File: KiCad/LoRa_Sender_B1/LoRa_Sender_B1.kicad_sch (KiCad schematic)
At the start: 5 parts, among them J1 Screw_Terminal_01x14, U1 RFM95W-868S2, U2 BME680

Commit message: Start design into KiCAD2
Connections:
- net GND: now also U2.1 (GND), U2.7 (GND)
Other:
- moved on the sheet: R1
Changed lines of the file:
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@@
 (kicad_sch (version 20230121) (generator eeschema)
   (paper "A4")
+  (junction (at 147.32 110.49) (diameter 0) (color 0 0 0 0)
+  )
   (wire (pts (xy 172.72 54.61) (xy 172.72 58.42))
     (stroke (width 0) (type default))
   )
+  (wire (pts (xy 147.32 110.49) (xy 147.32 118.11))
+    (stroke (width 0) (type default))
+  )
+  (wire (pts (xy 147.32 110.49) (xy 149.86 110.49))
+    (stroke (width 0) (type default))
+  )
   (wire (pts (xy 172.72 60.96) (xy 170.18 60.96))
     (stroke (width 0) (type default))
   )
   (wire (pts (xy 170.18 57.15) (xy 170.18 60.96))
+    (stroke (width 0) (type default))
+  )
+  (wire (pts (xy 144.78 110.49) (xy 147.32 110.49))
     (stroke (width 0) (type default))
   )
@@
     )
   )
-  (symbol (lib_id "Device:R_Photo") (at 113.03 67.31 0) (unit 1)
-    (in_bom yes) (on_board yes) (dnp no) (fields_autoplaced)
-    (property "Reference" "R1" (at 115.57 66.04 0)
-      (effects (font (size 1.27 1.27)) (justify left))
-    )
-    (property "Value" "R_Photo" (at 115.57 68.58 0)
-      (effects (font (size 1.27 1.27)) (justify left))
-    )
-    (property "Footprint" "" (at 114.3 73.66 90)
+  (symbol (lib_id "Device:R_Photo") (at 109.22 52.07 0) (unit 1)
+    (in_bom yes) (on_board yes) (dnp no) (fields_autoplaced)
+    (property "Reference" "R1" (at 111.76 50.8 0)
+      (effects (font (size 1.27 1.27)) (justify left))
+    )
+    (property "Value" "R_Photo" (at 111.76 53.34 0)
+      (effects (font (size 1.27 1.27)) (justify left))
+    )
+    (property "Footprint" "" (at 110.49 58.42 90)
       (effects (font (size 1.27 1.27)) (justify left) hide)
     )
-    (property "Datasheet" "~" (at 113.03 68.58 0)
+    (property "Datasheet" "~" (at 109.22 53.34 0)
       (effects (font (size 1.27 1.27)) hide)
     )
@@
     )
   )
-  (symbol (lib_id "power:GND") (at 62.23 72.39 0) (unit 1)
-    (in_bom yes) (on_board yes) (dnp no) (fields_autoplaced)
-    (property "Reference" "#PWR01" (at 62.23 78.74 0)
-      (effects (font (size 1.27 1.27)) hide)
-    )
-    (property "Value" "GND" (at 62.23 77.47 0)
-      (effects (font (size 1.27 1.27)))
-    )
-    (property "Footprint" "" (at 62.23 72.39 0)
-      (effects (font (size 1.27 1.27)) hide)
-    )
-    (property "Datasheet" "" (at 62.23 72.39 0)
+  (symbol (lib_id "power:GND") (at 147.32 118.11 0) (unit 1)
+    (in_bom yes) (on_board yes) (dnp no) (fields_autoplaced)
+    (property "Reference" "#PWR01" (at 147.32 124.46 0)
+      (effects (font (size 1.27 1.27)) hide)
+    )
+    (property "Value" "GND" (at 147.32 123.19 0)
+      (effects (font (size 1.27 1.27)))
+    )
+    (property "Footprint" "" (at 147.32 118.11 0)
+      (effects (font (size 1.27 1.27)) hide)
+    )
+    (property "Datasheet" "" (at 147.32 118.11 0)
       (effects (font (size 1.27 1.27)) hide)
     )
@@
       (effects (font (size 1.27 1.27)) hide)
     )
-    (property "Value" "+5V" (at 111.76 72.39 0)
-      (effects (font (size 1.27 1.27)))
-    )
+    (property "Value" "+5V" (at 175.26 52.07 0)
+      (effects (font (size 1.27 1.27)))
+    )

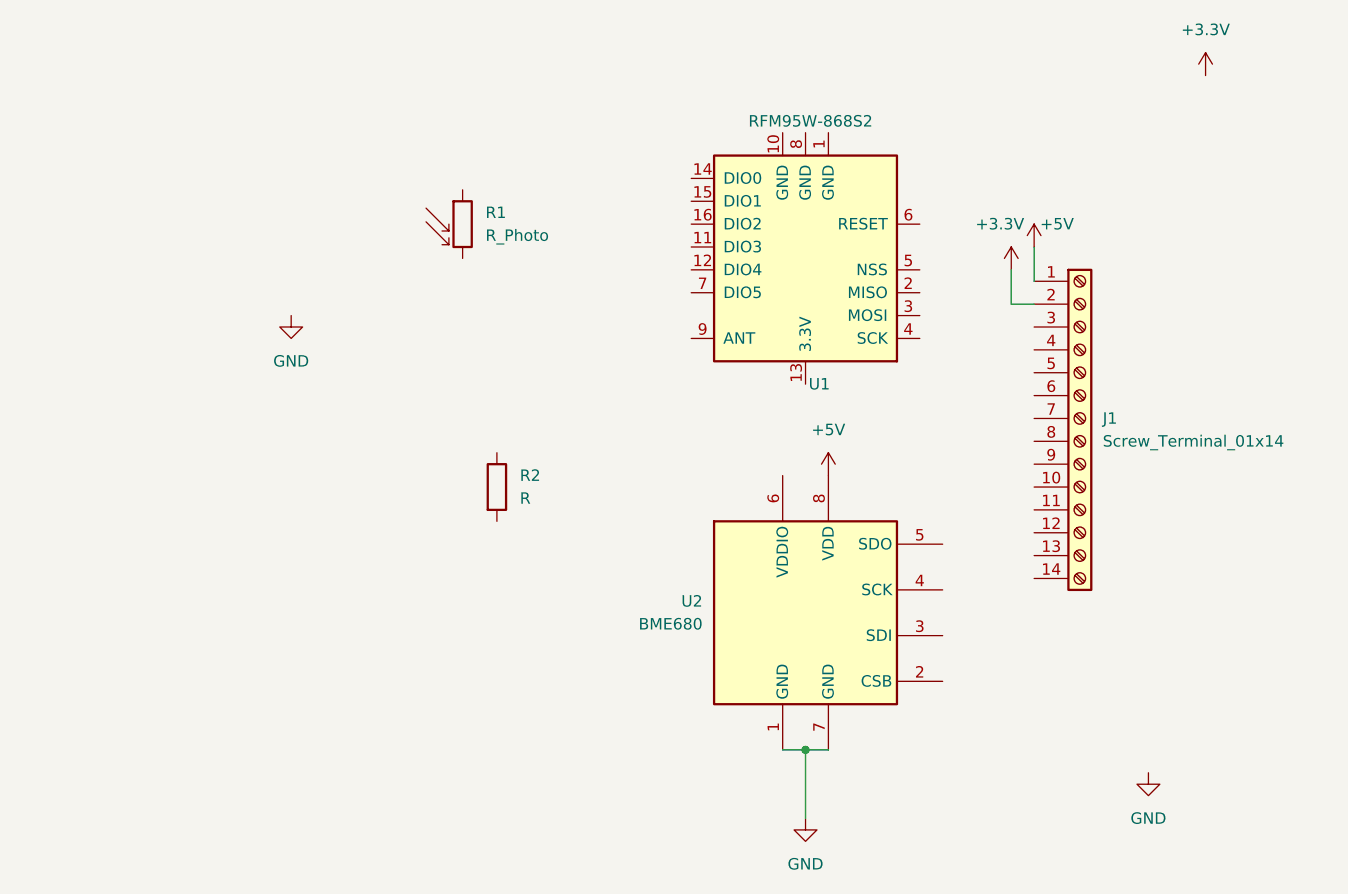
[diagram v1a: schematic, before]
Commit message: Start to create arduino wifi station code
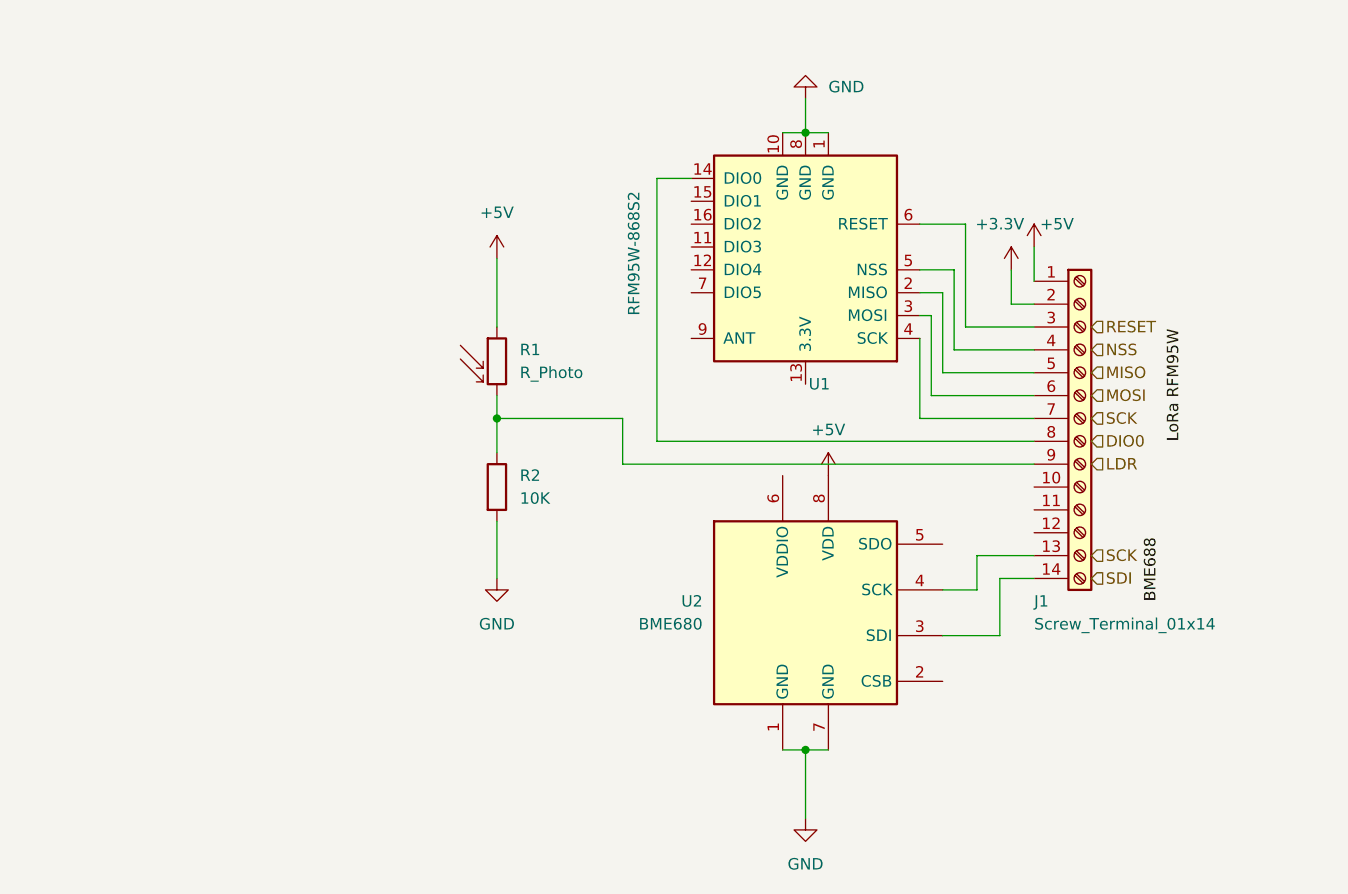
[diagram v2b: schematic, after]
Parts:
- R2: value R -> 10K
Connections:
- net +5V: now also R1.1
- net GND: now also R2.2, U1.1 (GND), U1.10 (GND), U1.8 (GND)
- net at J1.13 (Pin_13): now also U2.4 (SCK)
- net at J1.14 (Pin_14): now also U2.3 (SDI)
- net at J1.3 (Pin_3): now also U1.6 (RESET)
- net at J1.4 (Pin_4): now also U1.5 (NSS)
- net at J1.5 (Pin_5): now also U1.2 (MISO)
- net at J1.6 (Pin_6): now also U1.3 (MOSI)
- net at J1.7 (Pin_7): now also U1.4 (SCK)
- net at J1.8 (Pin_8): now also U1.14 (DIO0)
- net at J1.9 (Pin_9): now also R1.2, R2.1
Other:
- moved on the sheet: R1
